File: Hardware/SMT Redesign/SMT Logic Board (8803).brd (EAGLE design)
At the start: 83.8 x 43.4 mm, 32 parts, among them J4 KLDX-0202-B, SW1 FSMRA4JH04, SW2 FSMRA4JH04, SW3 5MS1S102AM6QES, U1 TLV76750QWDRBRQ1, U2 1364-HVPS-H, U3 PIC16F18444-E/GZ, U5 RV-8803-C7

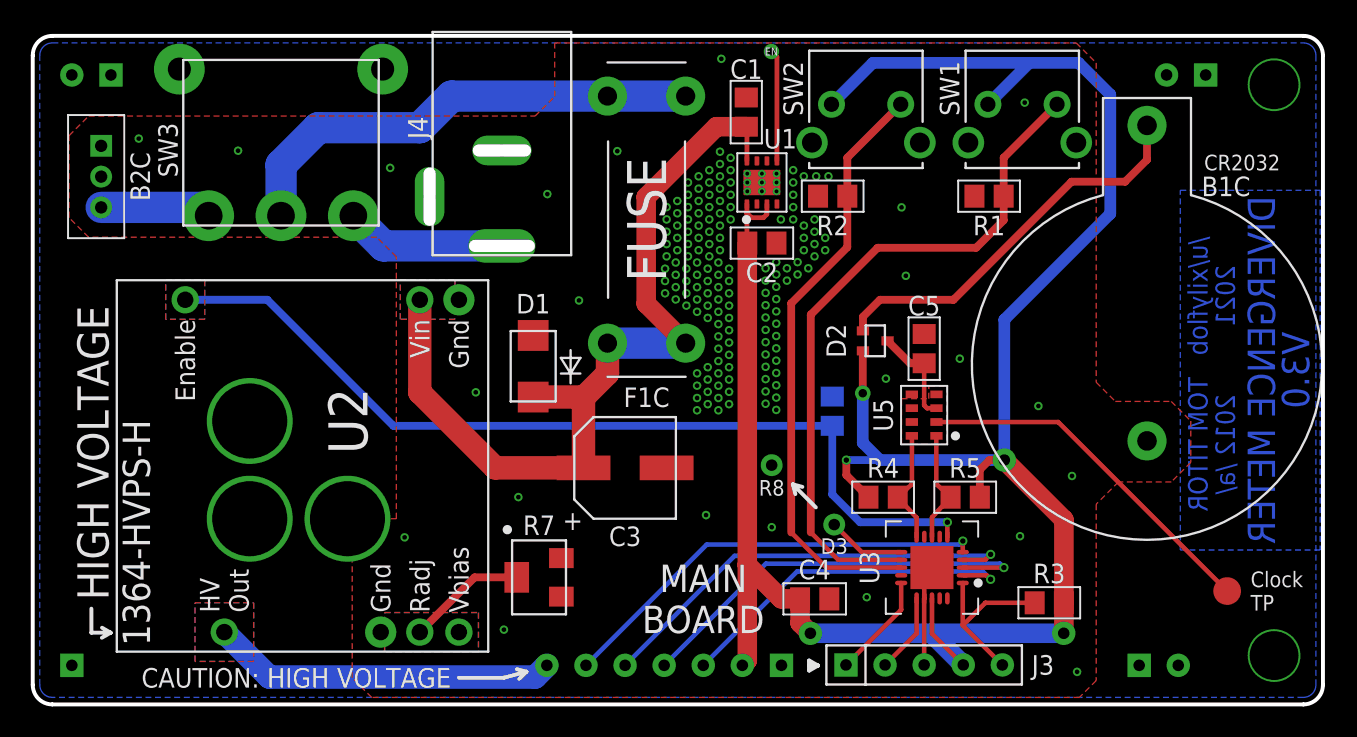
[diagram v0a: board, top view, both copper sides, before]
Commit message: Component numbering fix
There was a gap from U3 to U5, shifted U5 onwards down one (eg to U4).

Was also playing the with DR for JLCPCB, some pads etc may be wonky because of this.
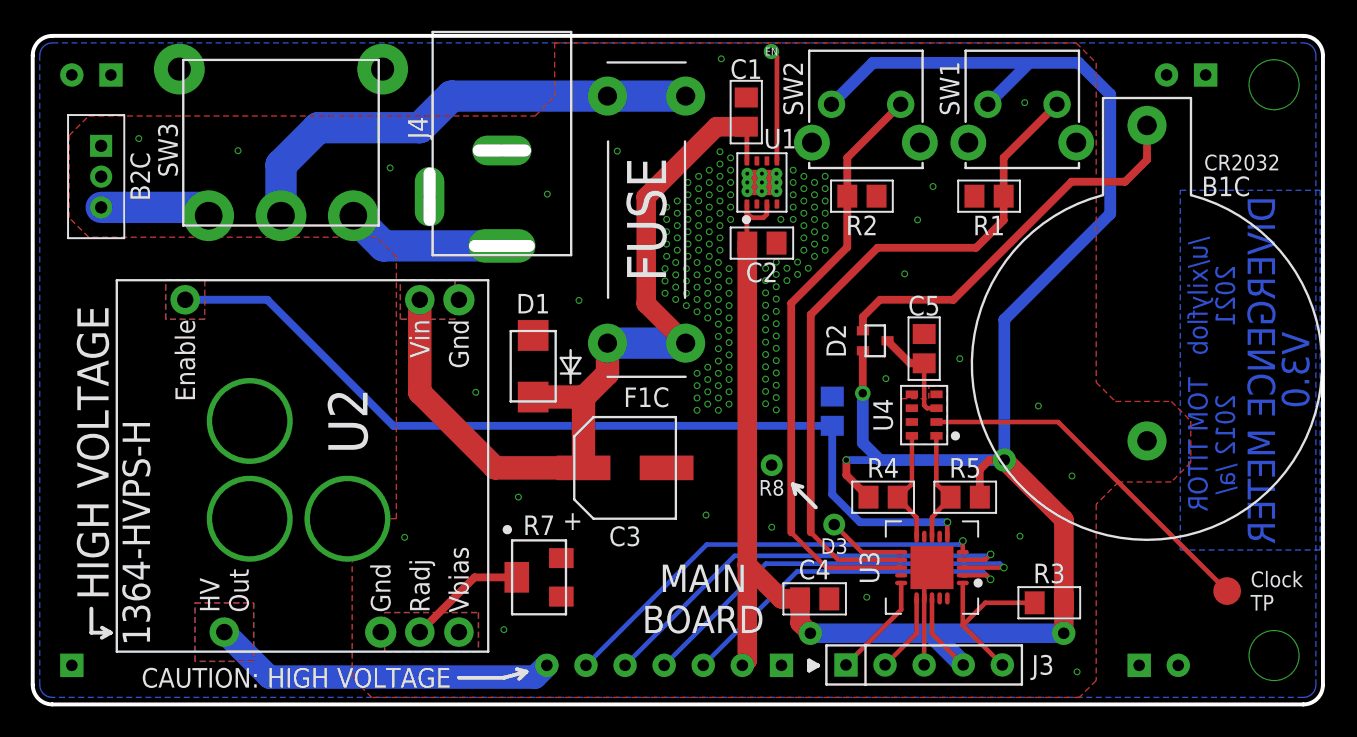
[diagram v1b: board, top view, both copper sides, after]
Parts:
- moved R2 1.90 mm to (53.9, 33.0), turned to 0 degrees
- renumbered U5 to U4
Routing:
- net GND: track 6.80 -> 6.54 mm, vias 173 -> 182
